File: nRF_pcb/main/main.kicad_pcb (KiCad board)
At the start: 2 copper layers, 46.5 x 38.5 mm, 7 parts, among them J1 SWD breakout, U1 XIAO-nRF52840-SMD, U2 SSD1306, U3 SM5308 LiPo, U4 BE-280, U5 SD Breakout

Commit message: Update PCB
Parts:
- added SW_CENTER1: SW_Push, diy_recreations:Button Center, F.Cu at (178.2, 90.0)
- added SW_LEFT1: SW_Push, diy_recreations:Button Left, F.Cu at (178.2, 99.0)
- added SW_RIGHT1: SW_Push, diy_recreations:Button Right, F.Cu at (178.0, 108.0)
- moved J1 3.66 mm to (169.5, 79.7)
- moved U2 3.66 mm to (169.5, 85.5)
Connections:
- net Net-(U1-P0.03_A1_D1) renamed /GPS_PPS
- net Net-(U1-P1.11_D6_TX) renamed /GPS_RX
- net Net-(U1-P1.12_D7_RX) renamed /GPS_TX
- net Net-(U1-P1.14_D9_MISO) renamed /SD_MISO
- net Net-(U1-P1.15_D10_MOSI) renamed /SD_MOSI
- U1 pad 3: unconnected-(U1-P0.28_A2_D2-Pad3) -> /BTN_CENTER
- U1 pad 4: unconnected-(U1-P0.29_A3_D3-Pad4) -> /SD_CS
- U5 pad 6: GND -> /SD_CS
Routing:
- net GND: track 14.2 -> 10.1 mm, vias 6 -> 4
- net /SD_CS: track 0.00 -> 2.08 mm, vias 0 -> 1
- net Net-(U1-P0.05_A5_D5_SCL): track 19.1 -> 17.5 mm
- net Net-(U1-P0.04_A4_D4_SDA): track 19.7 -> 18.5 mm
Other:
- board size 46.5 x 38.5 mm -> 56 x 38.5 mm

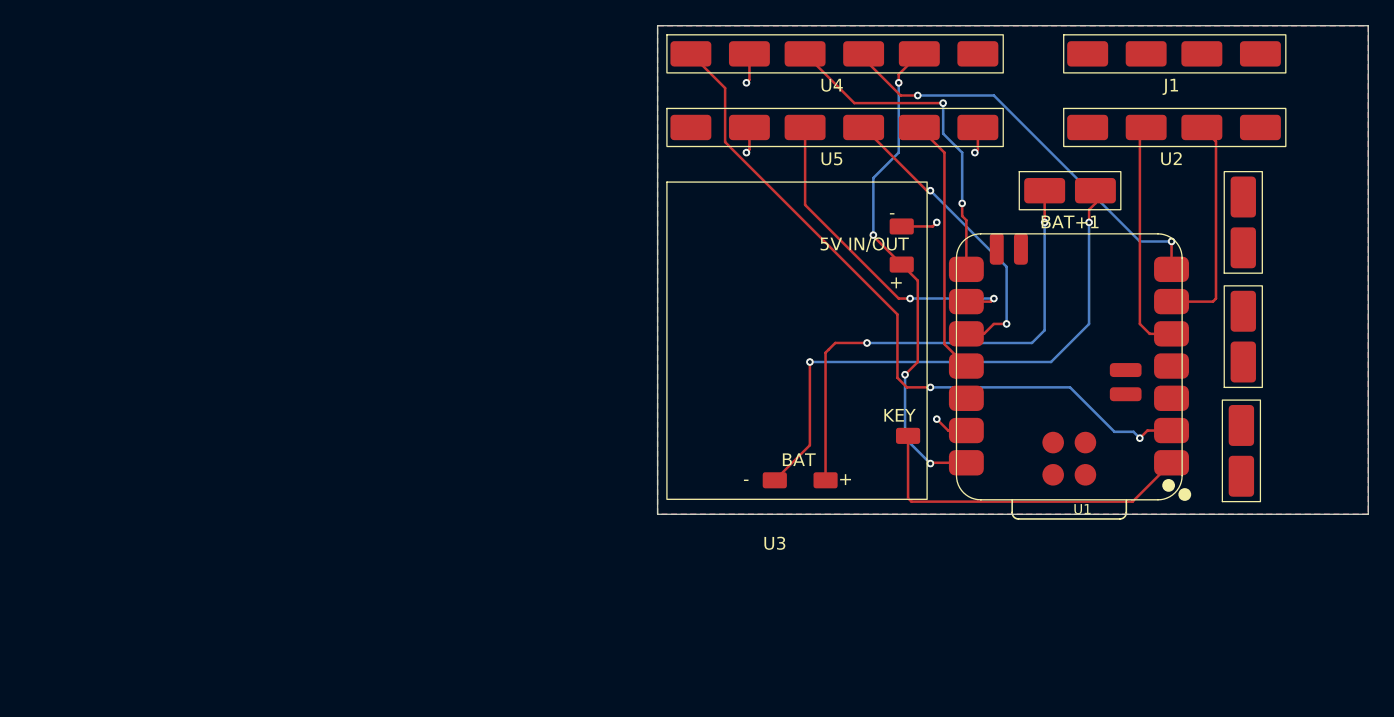
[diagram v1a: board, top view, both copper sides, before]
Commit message: Refactor to 3.3V only architecture
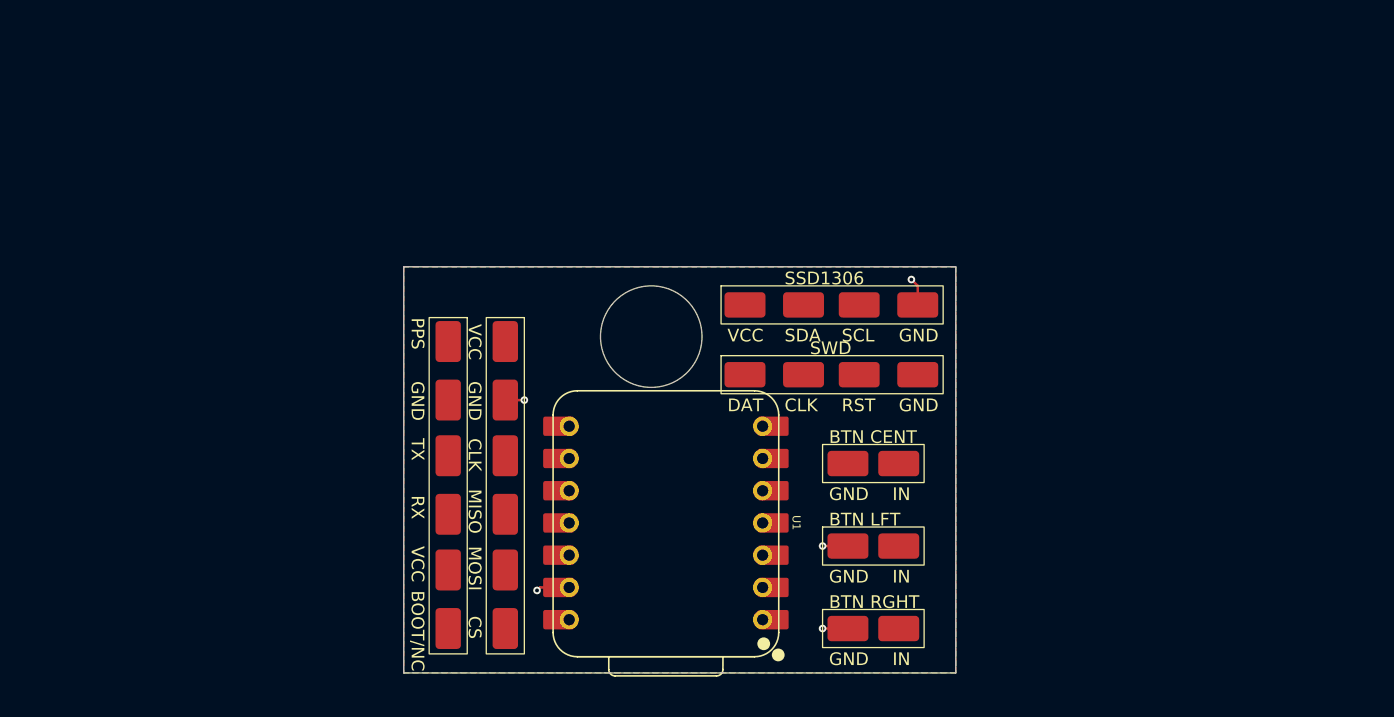
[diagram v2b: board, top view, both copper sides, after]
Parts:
- removed BAT+1: BAT-, diy_recreations:Battery Header
- removed U3: SM5308 LiPo, diy_recreations:SM5308 LiPo charger
- U1: footprint XIAO_Series_Footprints:XIAO-nRF52840-SMD -> XIAO_Series_Footprints:XIAO-nRF52840-DIP
- moved U1 46.7 mm to (129.7, 113.7), turned to -90 degrees
- moved U4 43.1 mm to (112.5, 110.5), turned to -90 degrees
- moved SW_CENTER1 37.3 mm to (146.0, 109.0), turned to 0 degrees
- moved SW_LEFT1 36.1 mm to (146.0, 115.5), turned to 0 degrees
- moved U5 35.9 mm to (117.0, 110.5), turned to -90 degrees
- moved J1 35.0 mm to (142.5, 102.0)
- moved SW_RIGHT1 34.9 mm to (146.0, 122.0), turned to 0 degrees
- moved U2 29.1 mm to (142.5, 96.5)
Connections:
- U1 pad 1: Net-(U1-P0.02_A0_D0) -> unconnected-(U1-P0.02_A0_D0-Pad1)_1
- U1 pad 14: +5V -> unconnected-(U1-VBUS-Pad14)
- U4 pad 5: +5V -> +3.3V
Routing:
- net /GPS_PPS: track 56.1 -> 0.00 mm, vias 2 -> 0
- net Net-(BAT+1-Pin_2): track 44.4 -> 0.00 mm, vias 2 -> 0
- net +5V: track 39.3 -> 0.00 mm, vias 4 -> 0
- net Net-(BAT+1-Pin_1): track 39.1 -> 0.00 mm, vias 2 -> 0
- net /GPS_RX: track 32.8 -> 0.00 mm, vias 2 -> 0
- net Net-(U1-P0.02_A0_D0): track 27.1 -> 0.00 mm
- net /GPS_TX: track 26.3 -> 0.00 mm, vias 2 -> 0
- net Net-(U1-P1.13_D8_SCK): track 26.3 -> 0.00 mm, vias 2 -> 0
- net /SD_MISO: track 23.8 -> 0.00 mm, vias 2 -> 0
- net /SD_MOSI: track 20.3 -> 0.00 mm
- net Net-(U1-P0.04_A4_D4_SDA): track 18.5 -> 0.00 mm
- net Net-(U1-P0.05_A5_D5_SCL): track 17.5 -> 0.00 mm
- net /SD_CS: track 2.08 -> 0.00 mm, vias 1 -> 0
- net GND: track 10.1 -> 9.51 mm, vias 4 -> 5
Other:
- board size 56 x 38.5 mm -> 43.5 x 32 mm

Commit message: Implement adafruit sd board footprint
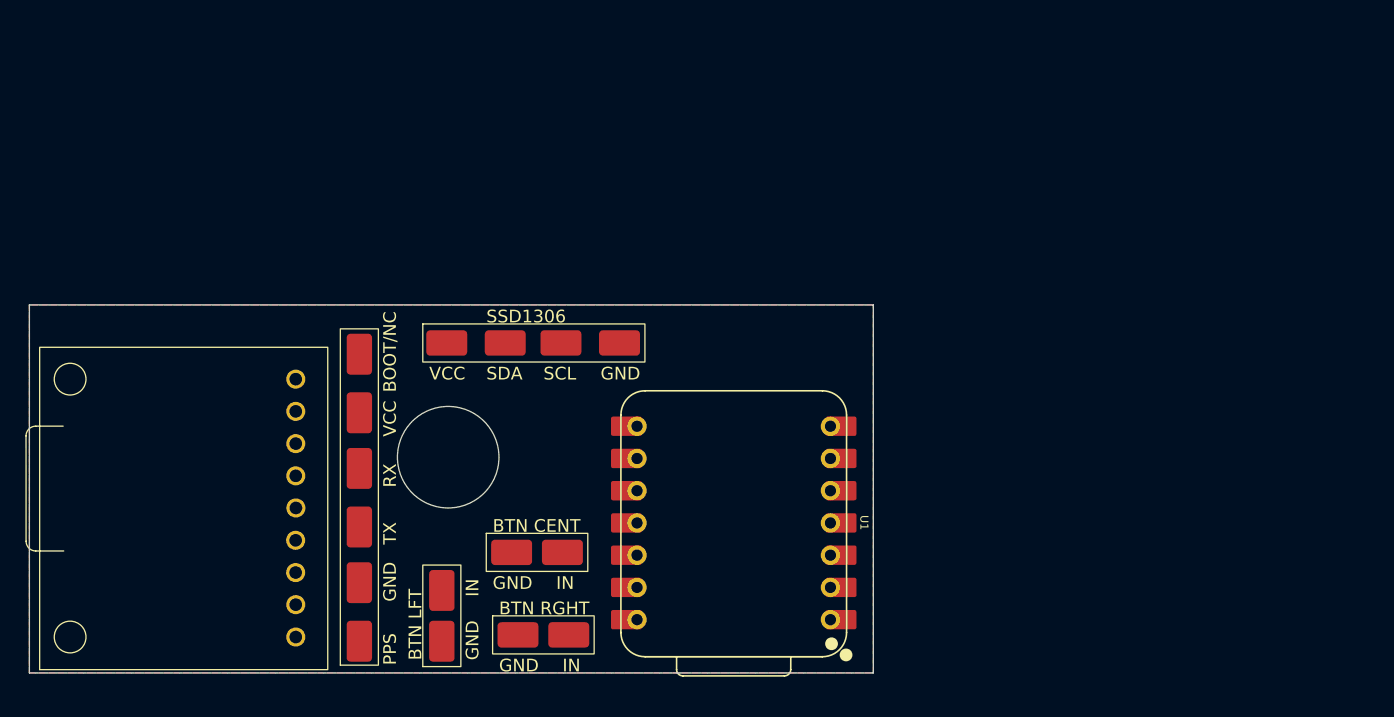
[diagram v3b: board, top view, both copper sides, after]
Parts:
- removed J1: SWD breakout, diy_recreations:SWD breakout
- moved SW_LEFT1 34.4 mm to (112.0, 121.0), turned to 90 degrees
- moved SW_CENTER1 27.4 mm to (119.5, 116.0)
- moved SW_RIGHT1 26.0 mm to (120.0, 122.5)
- moved U5 25.8 mm to (91.2, 111.8), turned to 90 degrees
- moved U2 23.7 mm to (119.0, 99.5)
- moved U4 7.14 mm to (105.5, 111.9), turned to 90 degrees
- moved U1 5.34 mm to (135.0, 113.7)
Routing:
- net GND: track 9.51 -> 0.00 mm, vias 5 -> 0
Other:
- board size 43.5 x 32 mm -> 66.5 x 29 mm

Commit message: Add 3V3 rail toggle
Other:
- outline, holes or cut-outs redrawn
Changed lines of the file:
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@@
 	)
 	(gr_circle
-		(center 112.5 108.5)
-		(end 108.5 108.5)
+		(center 114.5 108)
+		(end 109 108)
 		(stroke
 			(width 0.05)
